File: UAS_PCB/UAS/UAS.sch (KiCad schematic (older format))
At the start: 9 parts, among them J1 SM02B-PASS-TBT(LF)(SN), U1 7.5V-2.4A-Converter, U2 5A-5V-Converter, U3 500mA-5V-Converter, U4 12V-StepUp-Converter, U5 TB6612FNG-Dual-Motor-Driver

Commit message: Symbols oriented on schematic
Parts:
- removed J1: SM02B-PASS-TBT(LF)(SN), JST_SM02B-PASS-TBT(LF)(SN), symbol UAS-rescue:SM02B-PASS-TBT(LF)(SN)-SM02B-PASS-TBT_LF__SN_
- removed U1: 7.5V-2.4A-Converter, UAS:Pololu_7.75V_2.4A_Step_Down_Regulator, symbol UAS-rescue:7.5V-2.4A-Converter-UAS-cache
- removed U?: JST-4-Pin, symbol UAS-rescue:JST-4-Pin-UAS-cache
- added J? (x4): SM02B-PASS-TBT, symbol UAS-cache:SM02B-PASS-TBT
- added U?: JST-4-Pin, symbol UAS-rescue:JST-4-Pin-UAS-cache
- added U?: JST-3-Pin, symbol UAS-rescue:JST-3-Pin-UAS-cache
- added U?: JST-7-Pin, symbol UAS-rescue:JST-7-Pin-UAS-cache
- added U?: UAS-rescue_7.5V-2.4A-Converter-UAS-cache, symbol UAS-cache:UAS-rescue_7.5V-2.4A-Converter-UAS-cache
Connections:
- wire segments 0 -> 8
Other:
- moved on the sheet: U2, U3, U4, U5, U?
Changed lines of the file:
@@
 EESchema Schematic File Version 4
-LIBS:UAS-cache
 EELAYER 30 0
 EELAYER END
@@
 L UAS-rescue:500mA-5V-Converter-UAS-cache U3
 U 1 1 60360C06
-P 6100 2650
-F 0 "U3" H 6100 2725 50  0000 C CNN
-F 1 "500mA-5V-Converter" H 6100 2634 50  0000 C CNN
-F 2 "UAS:Pololu_5V_500mA_Step_Down_Regulator" H 6100 2750 50  0001 C CNN
-F 3 "" H 6100 2750 50  0001 C CNN
-	1    6100 2650
-	1    0    0    -1
-$EndComp
-$Comp
-L UAS-rescue:7.5V-2.4A-Converter-UAS-cache U1
-U 1 1 60361E55
-P 6100 3250
-F 0 "U1" H 6100 3315 50  0000 C CNN
-F 1 "7.5V-2.4A-Converter" H 6100 3224 50  0000 C CNN
-F 2 "UAS:Pololu_7.75V_2.4A_Step_Down_Regulator" H 6100 3350 50  0001 C CNN
-F 3 "" H 6100 3350 50  0001 C CNN
-	1    6100 3250
-	1    0    0    -1
-$EndComp
-$Comp
-L UAS-rescue:TB6612FNG-Dual-Motor-Driver-UAS-cache U5
-U 1 1 60364756
-P 6150 4150
-F 0 "U5" H 6150 4226 50  0000 C CNN
-F 1 "TB6612FNG-Dual-Motor-Driver" H 6150 4135 50  0000 C CNN
-F 2 "UAS:Pololu_TB6612_Dual_Motor_Driver_Carrier" H 6150 4250 50  0001 C CNN
-F 3 "" H 6150 4250 50  0001 C CNN
-	1    6150 4150
-	1    0    0    -1
-$EndComp
-$Comp
-L UAS-rescue:SM02B-PASS-TBT(LF)(SN)-SM02B-PASS-TBT_LF__SN_ J1
-U 1 1 60366780
-P 4850 2150
-F 0 "J1" H 5080 2146 50  0000 L CNN
-F 1 "SM02B-PASS-TBT(LF)(SN)" H 5080 2055 50  0000 L CNN
-F 2 "JST_SM02B-PASS-TBT(LF)(SN)" H 4850 2150 50  0001 L BNN
-F 3 "" H 4850 2150 50  0001 L BNN
-F 4 "N/A" H 4850 2150 50  0001 L BNN "PARTREV"
-F 5 "JST" H 4850 2150 50  0001 L BNN "MANUFACTURER"
-F 6 "Manufacturer Recommendations" H 4850 2150 50  0001 L BNN "STANDARD"
-F 7 "5.7 mm" H 4850 2150 50  0001 L BNN "MAXIMUM_PACKAGE_HEIGHT"
-	1    4850 2150
+P 9490 4805
+F 0 "U3" H 9490 4880 50  0000 C CNN
+F 1 "500mA-5V-Converter" H 9490 4789 50  0000 C CNN
+F 2 "UAS:Pololu_5V_500mA_Step_Down_Regulator" H 9490 4905 50  0001 C CNN
+F 3 "" H 9490 4905 50  0001 C CNN
+	1    9490 4805
 	1    0    0    -1
 $EndComp
@@
 L UAS-rescue:12V-StepUp-Converter-UAS-cache U4
 U 1 1 60363213
-P 6100 3700
-F 0 "U4" H 6100 3776 50  0000 C CNN
-F 1 "12V-StepUp-Converter" H 6100 3685 50  0000 C CNN
-F 2 "UAS:Pololu_12V_Step_Up_Voltage_Regulator" H 6100 3800 50  0001 C CNN
-F 3 "" H 6100 3800 50  0001 C CNN
-	1    6100 3700
+P 6165 4660
+F 0 "U4" H 6165 4736 50  0000 C CNN
+F 1 "12V-StepUp-Converter" H 6165 4645 50  0000 C CNN
+F 2 "UAS:Pololu_12V_Step_Up_Voltage_Regulator" H 6165 4760 50  0001 C CNN
+F 3 "" H 6165 4760 50  0001 C CNN
+	1    6165 4660
+	0    -1   -1   0
+$EndComp
+$Comp
+L UAS-rescue:JST-7-Pin-UAS-cache U?
+U 1 1 6036088A
+P 5325 3755
+F 0 "U?" H 5325 3830 50  0000 C CNN
+F 1 "JST-7-Pin" H 5325 3739 50  0000 C CNN
+F 2 "" H 5325 3855 50  0001 C CNN
+F 3 "" H 5325 3855 50  0001 C CNN
+	1    5325 3755
+	0    1    1    0
+$EndComp
+$Comp
+L UAS-rescue:JST-4-Pin-UAS-cache U?
+U 1 1 603691F2
+P 4985 5480
+F 0 "U?" H 4985 5555 50  0000 C CNN
+F 1 "JST-4-Pin" H 4985 5464 50  0000 C CNN
+F 2 "" H 4985 5580 50  0001 C CNN
+F 3 "" H 4985 5580 50  0001 C CNN
+	1    4985 5480
+	1    0    0    -1
+$EndComp
+$Comp
+L UAS-rescue:JST-3-Pin-UAS-cache U?
+U 1 1 6035FF82
+P 3970 5420
+F 0 "U?" H 3970 5495 50  0000 C CNN
+F 1 "JST-3-Pin" H 3970 5404 50  0000 C CNN
+F 2 "" H 3970 5520 50  0001 C CNN
+F 3 "" H 3970 5520 50  0001 C CNN
+	1    3970 5420
 	1    0    0    -1
 $EndComp
@@
 L UAS-rescue:5A-5V-Converter-UAS-cache U2
 U 1 1 6035F82F
-P 6100 1950
-F 0 "U2" H 6075 2025 50  0000 C CNN
-F 1 "5A-5V-Converter" H 6075 1934 50  0000 C CNN
-F 2 "UAS:Pololu_5V_5A_Step_Down_Regulator" H 6100 1950 50  0001 C CNN
-F 3 "" H 6100 1950 50  0001 C CNN
-	1    6100 1950
+P 5290 4690
+F 0 "U2" H 5265 4765 50  0000 C CNN
+F 1 "5A-5V-Converter" H 5265 4674 50  0000 C CNN
+F 2 "UAS:Pololu_5V_5A_Step_Down_Regulator" H 5290 4690 50  0001 C CNN
+F 3 "" H 5290 4690 50  0001 C CNN
+	1    5290 4690
+	0    1    1    0
+$EndComp
+$Comp
+L UAS-rescue:TB6612FNG-Dual-Motor-Driver-UAS-cache U5
+U 1 1 60364756
+P 4045 4295
+F 0 "U5" H 4045 4371 50  0000 C CNN
+F 1 "TB6612FNG-Dual-Motor-Driver" H 4045 4280 50  0000 C CNN
+F 2 "UAS:Pololu_TB6612_Dual_Motor_Driver_Carrier" H 4045 4395 50  0001 C CNN
+F 3 "" H 4045 4395 50  0001 C CNN
+	1    4045 4295
+	1    0    0    -1
+$EndComp
+$Comp
+L UAS-cache:SM02B-PASS-TBT J?
+U 1 1 6036D234
+P 3930 3745
+F 0 "J?" H 4058 3791 50  0000 L CNN
+F 1 "SM02B-PASS-TBT" H 4058 3700 50  0000 L CNN
+F 2 "" H 3930 3795 50  0001 L BNN
+F 3 "" H 3930 3795 50  0001 L BNN
+	1    3930 3745
+	1    0    0    -1
+$EndComp
+$Comp
+L UAS-cache:SM02B-PASS-TBT J?
+U 1 1 6036DBCC
+P 7015 3745
+F 0 "J?" H 7143 3791 50  0000 L CNN
+F 1 "SM02B-PASS-TBT" H 7143 3700 50  0000 L CNN
+F 2 "" H 7015 3795 50  0001 L BNN
+F 3 "" H 7015 3795 50  0001 L BNN
+	1    7015 3745
+	1    0    0    -1
+$EndComp
+$Comp
+L UAS-rescue:JST-7-Pin-UAS-cache U?
+U 1 1 60371401
+P 6090 3750
+F 0 "U?" H 6090 3825 50  0000 C CNN
+F 1 "JST-7-Pin" H 6090 3734 50  0000 C CNN
+F 2 "" H 6090 3850 50  0001 C CNN
+F 3 "" H 6090 3850 50  0001 C CNN
+	1    6090 3750
+	0    1    1    0
+$EndComp
+$Comp
+L UAS-cache:SM02B-PASS-TBT J?
+U 1 1 603683EB
+P 5895 5695
+F 0 "J?" H 6023 5741 50  0000 L CNN
+F 1 "SM02B-PASS-TBT" H 5535 5480 50  0000 L CNN
+F 2 "" H 5895 5745 50  0001 L BNN
+F 3 "" H 5895 5745 50  0001 L BNN
+	1    5895 5695
+	1    0    0    -1
+$EndComp
+$Comp
+L UAS-cache:UAS-rescue_7.5V-2.4A-Converter-UAS-cache U?
+U 1 1 6037F8BA
+P 5935 4775
+F 0 "U?" V 5864 4753 50  0000 L CNN
+F 1 "UAS-rescue_7.5V-2.4A-Converter-UAS-cache" V 5955 4753 50  0000 L CNN
+F 2 "" H 5935 4875 50  0001 C CNN
+F 3 "" H 5935 4875 50  0001 C CNN
+	1    5935 4775
+	0    1    1    0
+$EndComp
+$Comp
+L UAS-cache:SM02B-PASS-TBT J?
+U 1 1 60368871
+P 6495 5700
+F 0 "J?" H 6623 5746 50  0000 L CNN
+F 1 "SM02B-PASS-TBT" H 6150 5480 50  0000 L CNN
+F 2 "" H 6495 5750 50  0001 L BNN
+F 3 "" H 6495 5750 50  0001 L BNN
+	1    6495 5700
 	1    0    0    -1
 $EndComp
 $Comp
 L UAS-rescue:JST-3-Pin-UAS-cache U?
-U 1 1 6035FF82
-P 4150 2900
-F 0 "U?" H 4150 2975 50  0000 C CNN
-F 1 "JST-3-Pin" H 4150 2884 50  0000 C CNN
-F 2 "" H 4150 3000 50  0001 C CNN
-F 3 "" H 4150 3000 50  0001 C CNN
-	1    4150 2900
+U 1 1 60369E43
+P 7035 5660
+F 0 "U?" H 7035 5735 50  0000 C CNN
+F 1 "JST-3-Pin" H 7035 5644 50  0000 C CNN
+F 2 "" H 7035 5760 50  0001 C CNN
+F 3 "" H 7035 5760 50  0001 C CNN
+	1    7035 5660
 	1    0    0    -1
 $EndComp
-$Comp
-L UAS-rescue:JST-4-Pin-UAS-cache U?
-U 1 1 60360427
-P 4900 3150
-F 0 "U?" H 4900 3225 50  0000 C CNN
-F 1 "JST-4-Pin" H 4900 3134 50  0000 C CNN
-F 2 "" H 4900 3250 50  0001 C CNN
-F 3 "" H 4900 3250 50  0001 C CNN
-	1    4900 3150
-	1    0    0    -1
-$EndComp
-$Comp
-L UAS-rescue:JST-7-Pin-UAS-cache U?
-U 1 1 6036088A
-P 4450 3850
-F 0 "U?" H 4450 3925 50  0000 C CNN
-F 1 "JST-7-Pin" H 4450 3834 50  0000 C CNN
-F 2 "" H 4450 3950 50  0001 C CNN
-F 3 "" H 4450 3950 50  0001 C CNN
-	1    4450 3850
-	1    0    0    -1
-$EndComp
+Wire Wire Line
+	5180 5630 5185 5630
+Connection ~ 5185 5630
+Wire Wire Line
+	5185 5630 5300 5630
+Wire Wire Line
+	5180 5730 5185 5730
+Connection ~ 5185 5730
+Wire Wire Line
+	5185 5730 5300 5730
+Wire Wire Line
+	4790 5630 4785 5630
+Connection ~ 4785 5630
+Wire Wire Line
+	4785 5630 4650 5630
+Wire Wire Line
+	4790 5730 4785 5730
+Connection ~ 4785 5730
+Wire Wire Line
+	4785 5730 4650 5730
 $EndSCHEMATC

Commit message: schematic connections update
we need to fix these god awful connector symbols, sorry rani lol
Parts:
- removed U?: JST-4-Pin, symbol UAS-rescue:JST-4-Pin-UAS-cache
- added U?: UAS-rescue_JST-4-Pin-UAS-cache, symbol UAS-cache:UAS-rescue_JST-4-Pin-UAS-cache
- added U?: 16_Pad_2x8_Set, symbol UAS-cache:16_Pad_2x8_Set
- J? (x4): symbol UAS-cache:SM02B-PASS-TBT -> UAS-rescue:SM02B-PASS-TBT-UAS-cache
- U?: symbol UAS-cache:UAS-rescue_7.5V-2.4A-Converter-UAS-cache -> UAS-rescue:UAS-rescue_7.5V-2.4A-Converter-UAS-cache-UAS-cache
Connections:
- wire segments 8 -> 129
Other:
- moved on the sheet: U2, U3, U4, U5, U?

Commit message: Pad Symbol
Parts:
- U?: symbol UAS-cache:UAS-rescue_JST-4-Pin-UAS-cache -> UAS-rescue:UAS-rescue_JST-4-Pin-UAS-cache-UAS-cache
- U?: symbol UAS-cache:16_Pad_2x8_Set -> UAS-rescue:16_Pad_2x8_Set-UAS-cache
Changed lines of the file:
@@
 	2100 4800 2100 5250
 $Comp
-L UAS-cache:UAS-rescue_JST-4-Pin-UAS-cache U?
+L UAS-rescue:UAS-rescue_JST-4-Pin-UAS-cache-UAS-cache U?
 U 1 1 6037EE1D
 P 3000 6150
@@
 	2500 2800 2500 3250
 $Comp
-L UAS-cache:16_Pad_2x8_Set U?
+L UAS-rescue:16_Pad_2x8_Set-UAS-cache U?
 U 1 1 6040B9AA
 P 2550 3050

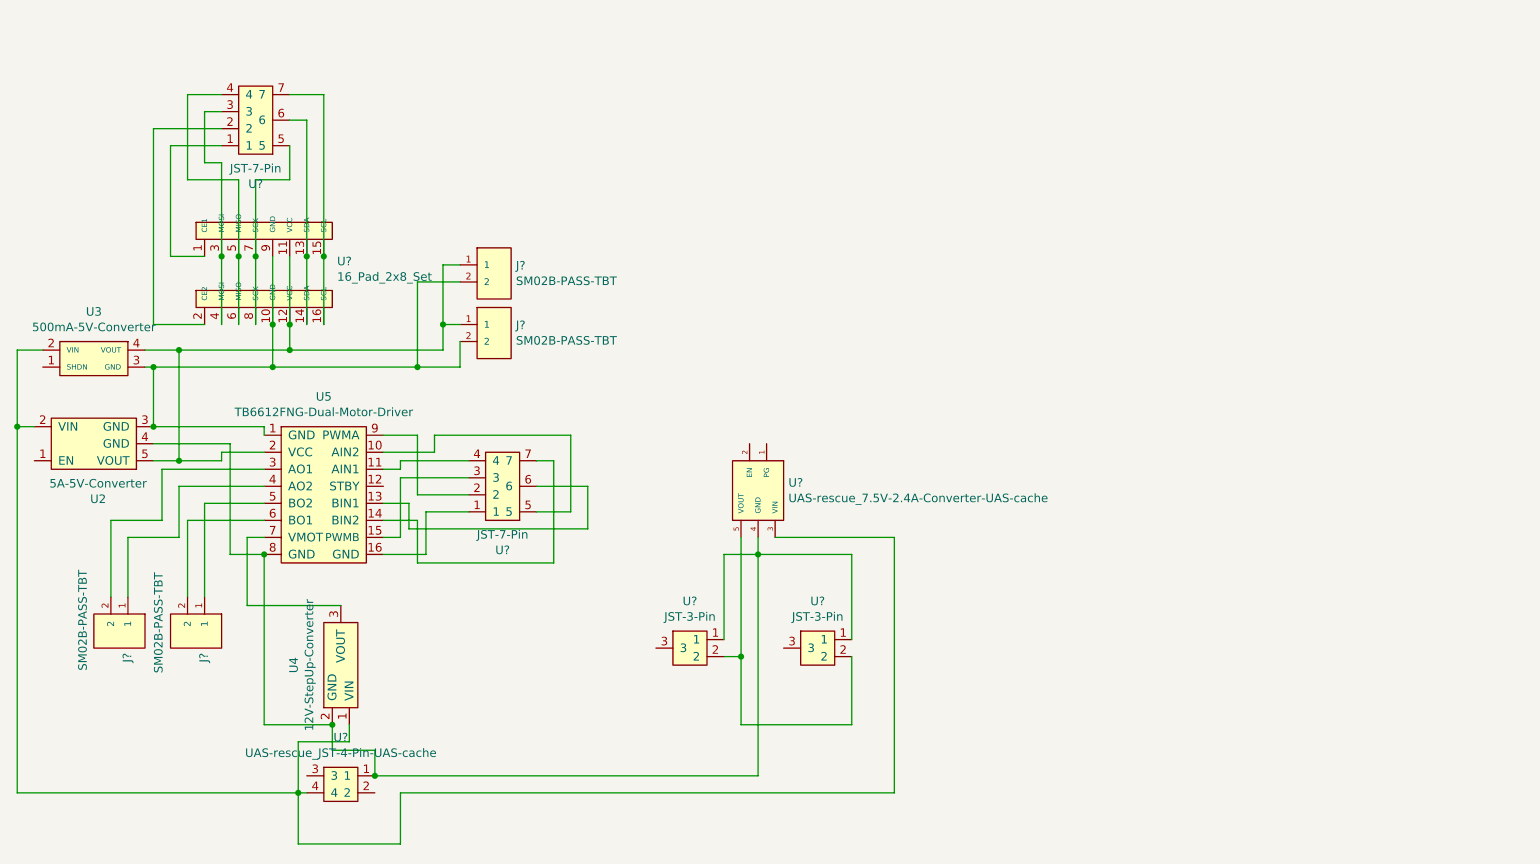
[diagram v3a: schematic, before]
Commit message: First Layout Attempt and Updated Footprints
needs a rework and a dimension change/shape change
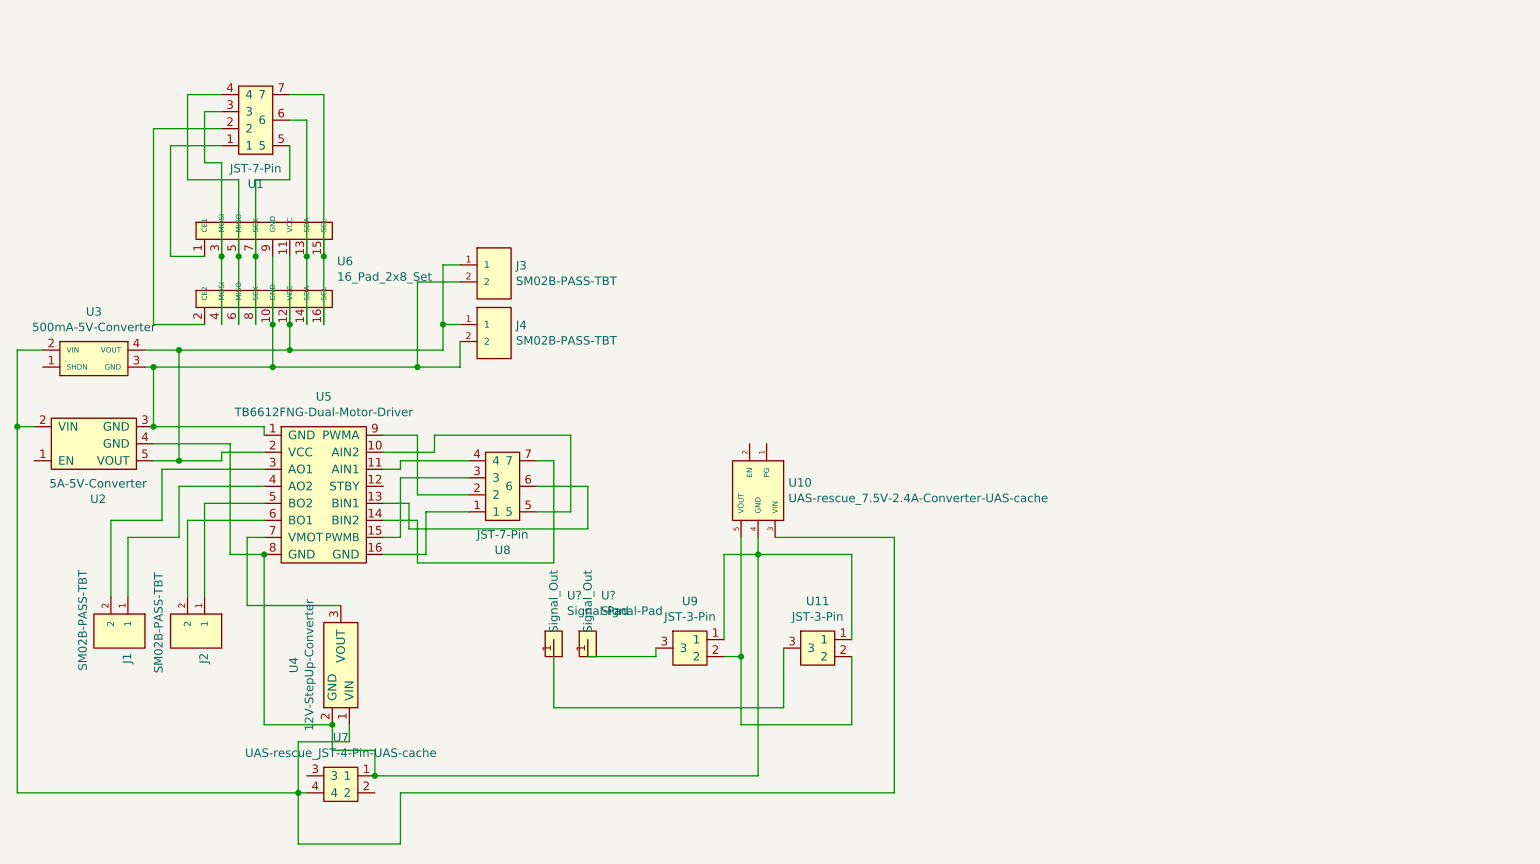
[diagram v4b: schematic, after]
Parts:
- added U? (x2): Signal-Pad, symbol UAS-cache:Signal-Pad
- J1, J2, J3, J4: renamed from J?; footprint (none) -> UAS:JST_SM02B-PASS-TBT(LF)(SN)
- U1, U8: renamed from U?; footprint (none) -> UAS:JST_SM07B-PASS-TBT(LF)(SN)
- U10: renamed from U?; footprint (none) -> UAS:Pololu_7.75V_2.4A_Step_Down_Regulator
- U11, U9: renamed from U?; footprint (none) -> UAS:JST_SM03B-PASS-TBT(LF)(SN)
- U6: renamed from U?; footprint (none) -> UAS:16_Pad_Set_2mm_pitch
- U7: renamed from U?; footprint (none) -> UAS:JST_XH_B4B-XH-A_1x04_P2.50mm_Vertical
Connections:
- net at U9.3: now also U?.1 (Signal_Out)
- net at U11.3: now also U?.1 (Signal_Out)
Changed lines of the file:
@@
 $EndComp
 $Comp
-L UAS-rescue:JST-7-Pin-UAS-cache U?
+L UAS-rescue:JST-7-Pin-UAS-cache U8
 U 1 1 6036088A
 P 3950 4900
-F 0 "U?" H 3950 4975 50  0000 C CNN
+F 0 "U8" H 3950 4975 50  0000 C CNN
 F 1 "JST-7-Pin" H 3950 4884 50  0000 C CNN
-F 2 "" H 3950 5000 50  0001 C CNN
+F 2 "UAS:JST_SM07B-PASS-TBT(LF)(SN)" H 3950 5000 50  0001 C CNN
 F 3 "" H 3950 5000 50  0001 C CNN
 	1    3950 4900
@@
 $EndComp
 $Comp
-L UAS-rescue:JST-3-Pin-UAS-cache U?
+L UAS-rescue:JST-3-Pin-UAS-cache U9
 U 1 1 6035FF82
 P 5050 5350
-F 0 "U?" H 5050 5425 50  0000 C CNN
+F 0 "U9" H 5050 5425 50  0000 C CNN
 F 1 "JST-3-Pin" H 5050 5334 50  0000 C CNN
-F 2 "" H 5050 5450 50  0001 C CNN
+F 2 "UAS:JST_SM03B-PASS-TBT(LF)(SN)" H 5050 5450 50  0001 C CNN
 F 3 "" H 5050 5450 50  0001 C CNN
 	1    5050 5350
@@
 $EndComp
 $Comp
-L UAS-rescue:SM02B-PASS-TBT-UAS-cache J?
+L UAS-rescue:SM02B-PASS-TBT-UAS-cache J4
 U 1 1 6036D234
 P 3900 3700
-F 0 "J?" H 4028 3746 50  0000 L CNN
+F 0 "J4" H 4028 3746 50  0000 L CNN
 F 1 "SM02B-PASS-TBT" H 4028 3655 50  0000 L CNN
-F 2 "" H 3900 3750 50  0001 L BNN
+F 2 "UAS:JST_SM02B-PASS-TBT(LF)(SN)" H 3900 3750 50  0001 L BNN
 F 3 "" H 3900 3750 50  0001 L BNN
 	1    3900 3700
@@
 $EndComp
 $Comp
-L UAS-rescue:SM02B-PASS-TBT-UAS-cache J?
+L UAS-rescue:SM02B-PASS-TBT-UAS-cache J3
 U 1 1 6036DBCC
 P 3900 3350
-F 0 "J?" H 4028 3396 50  0000 L CNN
+F 0 "J3" H 4028 3396 50  0000 L CNN
 F 1 "SM02B-PASS-TBT" H 4028 3305 50  0000 L CNN
-F 2 "" H 3900 3400 50  0001 L BNN
+F 2 "UAS:JST_SM02B-PASS-TBT(LF)(SN)" H 3900 3400 50  0001 L BNN
 F 3 "" H 3900 3400 50  0001 L BNN
 	1    3900 3350
@@
 $EndComp
 $Comp
-L UAS-rescue:JST-7-Pin-UAS-cache U?
+L UAS-rescue:JST-7-Pin-UAS-cache U1
 U 1 1 60371401
 P 2500 2750
-F 0 "U?" H 2500 2825 50  0000 C CNN
+F 0 "U1" H 2500 2825 50  0000 C CNN
 F 1 "JST-7-Pin" H 2500 2734 50  0000 C CNN
-F 2 "" H 2500 2850 50  0001 C CNN
+F 2 "UAS:JST_SM07B-PASS-TBT(LF)(SN)" H 2500 2850 50  0001 C CNN
 F 3 "" H 2500 2850 50  0001 C CNN
 	1    2500 2750
@@
 $EndComp
 $Comp
-L UAS-rescue:SM02B-PASS-TBT-UAS-cache J?
+L UAS-rescue:SM02B-PASS-TBT-UAS-cache J1
 U 1 1 603683EB
 P 1700 5450
-F 0 "J?" H 1828 5496 50  0000 L CNN
+F 0 "J1" H 1828 5496 50  0000 L CNN
 F 1 "SM02B-PASS-TBT" H 1340 5235 50  0000 L CNN
-F 2 "" H 1700 5500 50  0001 L BNN
+F 2 "UAS:JST_SM02B-PASS-TBT(LF)(SN)" H 1700 5500 50  0001 L BNN
 F 3 "" H 1700 5500 50  0001 L BNN
 	1    1700 5450
@@
 $EndComp
 $Comp
-L UAS-rescue:UAS-rescue_7.5V-2.4A-Converter-UAS-cache-UAS-cache U?
+L UAS-rescue:UAS-rescue_7.5V-2.4A-Converter-UAS-cache-UAS-cache U10
 U 1 1 6037F8BA
 P 5650 4650
-F 0 "U?" V 5579 4628 50  0000 L CNN
+F 0 "U10" V 5579 4628 50  0000 L CNN
 F 1 "UAS-rescue_7.5V-2.4A-Converter-UAS-cache" V 5670 4628 50  0000 L CNN
-F 2 "" H 5650 4750 50  0001 C CNN
+F 2 "UAS:Pololu_7.75V_2.4A_Step_Down_Regulator" H 5650 4750 50  0001 C CNN
 F 3 "" H 5650 4750 50  0001 C CNN
 	1    5650 4650
@@
 $EndComp
 $Comp
-L UAS-rescue:SM02B-PASS-TBT-UAS-cache J?
+L UAS-rescue:SM02B-PASS-TBT-UAS-cache J2
 U 1 1 60368871
 P 2150 5450
-F 0 "J?" H 2278 5496 50  0000 L CNN
+F 0 "J2" H 2278 5496 50  0000 L CNN
 F 1 "SM02B-PASS-TBT" H 1805 5230 50  0000 L CNN
-F 2 "" H 2150 5500 50  0001 L BNN
+F 2 "UAS:JST_SM02B-PASS-TBT(LF)(SN)" H 2150 5500 50  0001 L BNN
 F 3 "" H 2150 5500 50  0001 L BNN
 	1    2150 5450
@@
 $EndComp
 $Comp
-L UAS-rescue:JST-3-Pin-UAS-cache U?
+L UAS-rescue:JST-3-Pin-UAS-cache U11
 U 1 1 60369E43
 P 5800 5350
-F 0 "U?" H 5800 5425 50  0000 C CNN
+F 0 "U11" H 5800 5425 50  0000 C CNN
 F 1 "JST-3-Pin" H 5800 5334 50  0000 C CNN
-F 2 "" H 5800 5450 50  0001 C CNN
+F 2 "UAS:JST_SM03B-PASS-TBT(LF)(SN)" H 5800 5450 50  0001 C CNN
 F 3 "" H 5800 5450 50  0001 C CNN
 	1    5800 5350
@@
 	2100 4800 2100 5250
 $Comp
-L UAS-rescue:UAS-rescue_JST-4-Pin-UAS-cache-UAS-cache U?
+L UAS-rescue:UAS-rescue_JST-4-Pin-UAS-cache-UAS-cache U7
 U 1 1 6037EE1D
 P 3000 6150
-F 0 "U?" H 3000 6225 50  0000 C CNN
+F 0 "U7" H 3000 6225 50  0000 C CNN
 F 1 "UAS-rescue_JST-4-Pin-UAS-cache" H 3000 6134 50  0000 C CNN
-F 2 "" H 3000 6250 50  0001 C CNN
+F 2 "UAS:JST_XH_B4B-XH-A_1x04_P2.50mm_Vertical" H 3000 6250 50  0001 C CNN
 F 3 "" H 3000 6250 50  0001 C CNN
 	1    3000 6150
@@
 	2500 2800 2500 3250
 $Comp
-L UAS-rescue:16_Pad_2x8_Set-UAS-cache U?
+L UAS-rescue:16_Pad_2x8_Set-UAS-cache U6
 U 1 1 6040B9AA
 P 2550 3050
-F 0 "U?" H 2978 2821 50  0000 L CNN
+F 0 "U6" H 2978 2821 50  0000 L CNN
 F 1 "16_Pad_2x8_Set" H 2978 2730 50  0000 L CNN
-F 2 "" H 2550 3050 50  0001 C CNN
+F 2 "UAS:16_Pad_Set_2mm_pitch" H 2550 3050 50  0001 C CNN
 F 3 "" H 2550 3050 50  0001 C CNN
 	1    2550 3050
@@
 	2900 3650 2900 3250
 Connection ~ 2900 3250
+$Comp
+L UAS-cache:Signal-Pad U?
+U 1 1 60391DEE
+P 4250 5500
+F 0 "U?" H 4328 5759 50  0000 L CNN
+F 1 "Signal-Pad" H 4328 5668 50  0000 L CNN
+F 2 "" H 4250 5500 50  0001 C CNN
+F 3 "" H 4250 5500 50  0001 C CNN
+	1    4250 5500
+	1    0    0    -1
+$EndComp
+$Comp
+L UAS-cache:Signal-Pad U?
+U 1 1 60392D35
+P 4450 5500
+F 0 "U?" H 4528 5759 50  0000 L CNN
+F 1 "Signal-Pad" H 4528 5668 50  0000 L CNN
+F 2 "" H 4450 5500 50  0001 C CNN
+F 3 "" H 4450 5500 50  0001 C CNN
+	1    4450 5500
+	1    0    0    -1
+$EndComp
+Wire Wire Line
+	4450 5600 4850 5600
+Wire Wire Line
+	4850 5600 4850 5550
+Wire Wire Line
+	4250 5600 4250 5900
+Wire Wire Line
+	4250 5900 5600 5900
+Wire Wire Line
+	5600 5900 5600 5550
 $EndSCHEMATC

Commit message: added PWM signal testpad
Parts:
- U? (x2): footprint (none) -> UAS:Individual_Solder_Pad; symbol UAS-cache:Signal-Pad -> UAS-rescue:Signal-Pad-UAS-cache
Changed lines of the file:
@@
 Connection ~ 2900 3250
 $Comp
-L UAS-cache:Signal-Pad U?
+L UAS-rescue:Signal-Pad-UAS-cache U?
 U 1 1 60391DEE
 P 4250 5500
 F 0 "U?" H 4328 5759 50  0000 L CNN
 F 1 "Signal-Pad" H 4328 5668 50  0000 L CNN
-F 2 "" H 4250 5500 50  0001 C CNN
+F 2 "UAS:Individual_Solder_Pad" H 4250 5500 50  0001 C CNN
 F 3 "" H 4250 5500 50  0001 C CNN
 	1    4250 5500
@@
 $EndComp
 $Comp
-L UAS-cache:Signal-Pad U?
+L UAS-rescue:Signal-Pad-UAS-cache U?
 U 1 1 60392D35
 P 4450 5500
 F 0 "U?" H 4528 5759 50  0000 L CNN
 F 1 "Signal-Pad" H 4528 5668 50  0000 L CNN
-F 2 "" H 4450 5500 50  0001 C CNN
+F 2 "UAS:Individual_Solder_Pad" H 4450 5500 50  0001 C CNN
 F 3 "" H 4450 5500 50  0001 C CNN
 	1    4450 5500
 	1    0    0    -1
 $EndComp
-Wire Wire Line
-	4450 5600 4850 5600
-Wire Wire Line
-	4850 5600 4850 5550
 Wire Wire Line
 	4250 5600 4250 5900
@@
 Wire Wire Line
 	5600 5900 5600 5550
+Wire Wire Line
+	4850 5550 4850 5700
+Wire Wire Line
+	4850 5700 4450 5700
+Wire Wire Line
+	4450 5700 4450 5600
 $EndSCHEMATC
